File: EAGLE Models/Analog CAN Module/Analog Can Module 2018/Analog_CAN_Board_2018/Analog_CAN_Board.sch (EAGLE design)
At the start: 121 parts, among them IC1 AT90CAN128, IC10 OPA725DBV, IC11 OPA725DBV, IC12 OPA725DBV, IC13 OPA725DBV, IC2 MCP2551SO8, IC3 NUP2105L, IC4 OPA725DBV, IC5 FT232RL, IC6 MAX680CSA, IC7 OPA725DBV, IC8 OPA725DBV, IC9 OPA725DBV, Q1 56P2859, U11 LTC2053

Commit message: CAN Boards Finished
Passes DFM!
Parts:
- removed D1: 1N5819, diode:1N5819-B
- added U$4: 1N5819, diode:1N5819
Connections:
- net 12V: now also U$4.A; no longer D1.A
- net 5V_REG_IN: now also U$4.C; no longer D1.C
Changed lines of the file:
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@@
 <?xml version="1.0" encoding="utf-8"?>
 <!DOCTYPE eagle SYSTEM "eagle.dtd">
-<eagle version="8.4.2">
+<eagle version="8.3.2">
 <drawing>
 <settings>
@@
 <part name="D3" library="adafruit" deviceset="DIODE" device="SOD-123" value="1N4148"/>
 <part name="SJ2" library="SparkFun-Passives" deviceset="SOLDERJUMPER" device="NO"/>
-<part name="D1" library="diode" deviceset="1N581*" device="" technology="9-B" value="1N5819"/>
 <part name="U$26" library="on-semiconductor" deviceset="NCP1117" device=""/>
 <part name="C23" library="rcl" deviceset="C-US" device="C0603" value="10uF"/>
@@
 <part name="R37" library="SparkFun-Resistors" deviceset="RESISTOR" device="0603" value="0"/>
 <part name="U$1" library="us-te-con" deviceset="1734753-1_MINIUSB_CON" device=""/>
+<part name="U$4" library="diode" deviceset="1N5819" device=""/>
 </parts>
 <sheets>
@@
 <instance part="D3" gate="G$1" x="480.06" y="-106.68" rot="R90"/>
 <instance part="SJ2" gate="1" x="454.66" y="-114.3"/>
-<instance part="D1" gate="G$1" x="40.64" y="-30.48"/>
 <instance part="U$26" gate="G$1" x="78.74" y="-30.48"/>
 <instance part="C23" gate="G$1" x="50.8" y="-38.1"/>
@@
 <instance part="R37" gate="G$1" x="525.78" y="-40.64" rot="R270"/>
 <instance part="U$1" gate="G$1" x="378.46" y="-185.42"/>
+<instance part="U$4" gate="G$1" x="40.64" y="-30.48"/>
 </instances>
 <busses>
@@
 </segment>
 <segment>
-<pinref part="D1" gate="G$1" pin="A"/>
 <wire x1="38.1" y1="-30.48" x2="30.48" y2="-30.48" width="0.1524" layer="91"/>
 <label x="30.48" y="-30.48" size="1.778" layer="95" rot="R180" xref="yes"/>
+<pinref part="U$4" gate="G$1" pin="A"/>
 </segment>
 <segment>
@@
 <pinref part="U$26" gate="G$1" pin="INPUT"/>
 <wire x1="50.8" y1="-30.48" x2="63.5" y2="-30.48" width="0.1524" layer="91"/>
-<pinref part="D1" gate="G$1" pin="C"/>
 <wire x1="43.18" y1="-30.48" x2="50.8" y2="-30.48" width="0.1524" layer="91"/>
 <junction x="50.8" y="-30.48"/>
-</segment>
-</net>
+<pinref part="U$4" gate="G$1" pin="C"/>
+</segment>
+</net>

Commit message: Last minute CAN Board revision
- added 0 ohm resistors for filters and adjusted q to 2
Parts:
- added R36, R38, R39, R40, R41, R42, R43, R44: 0, SparkFun-Resistors:RESISTOR0603
- C14, C21, C27, C3, C35, C41, C45: value .1uF -> .0047uF
- C17, C26, C30, C44, C48, C6: value .33uF -> .1uF
- R1, R14, R17, R20, R26, R30, R33: value 3.9k -> 22k
- R16, R19, R22, R28, R29, R32, R35: value 5.1k -> 62k
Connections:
- net AGND: now also R36.2, R38.2, R39.2, R40.2, R41.2, R42.2, R43.2, R44.2
- net N$19: now also R36.1
- net N$26: now also R38.1
- net N$31: now also R39.1
- net N$38: now also R40.1
- net N$41: now also R44.1
- net N$44: now also R43.1
- net N$47: now also R42.1
- net N$50: now also R41.1
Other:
- moved on the sheet: C14, C15, C16, C17, C21, C22, C25, C26, C27, C28, C29, C3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

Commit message: Analog CAN Board Update
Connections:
- net AGND: now also U$3.B22, U$3.B23, U$3.B24; no longer U$3.B14, U$3.B15
- net DGND: now also U$3.B14, U$3.B15; no longer U$3.B22, U$3.B23, U$3.B24
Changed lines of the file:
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@@
-</segment>
-<segment>
-<pinref part="U$3" gate="G$1" pin="B14"/>
-<wire x1="495.3" y1="-15.24" x2="497.84" y2="-15.24" width="0.1524" layer="91"/>
-<label x="497.84" y="-15.24" size="1.778" layer="95"/>
-</segment>
-<segment>
-<pinref part="U$3" gate="G$1" pin="B15"/>
-<wire x1="495.3" y1="-20.32" x2="497.84" y2="-20.32" width="0.1524" layer="91"/>
-<label x="497.84" y="-20.32" size="1.778" layer="95"/>
 </segment>
 <segment>
@@
 <wire x1="347.98" y1="12.7" x2="342.9" y2="12.7" width="0.1524" layer="91"/>
 <label x="342.9" y="12.7" size="1.4224" layer="95" rot="R180" xref="yes"/>
+</segment>
+<segment>
+<pinref part="U$3" gate="G$1" pin="B24"/>
+<wire x1="495.3" y1="-66.04" x2="497.84" y2="-66.04" width="0.1524" layer="91"/>
+<label x="497.84" y="-66.04" size="1.778" layer="95"/>
+</segment>
+<segment>
+<pinref part="U$3" gate="G$1" pin="B23"/>
+<wire x1="495.3" y1="-60.96" x2="497.84" y2="-60.96" width="0.1524" layer="91"/>
+<label x="497.84" y="-60.96" size="1.778" layer="95"/>
+</segment>
+<segment>
+<pinref part="U$3" gate="G$1" pin="B22"/>
+<wire x1="495.3" y1="-55.88" x2="497.84" y2="-55.88" width="0.1524" layer="91"/>
+<label x="497.84" y="-55.88" size="1.778" layer="95"/>
 </segment>
 </net>
@@
 </segment>
 <segment>
-<pinref part="U$3" gate="G$1" pin="B22"/>
-<wire x1="495.3" y1="-55.88" x2="497.84" y2="-55.88" width="0.1524" layer="91"/>
-<label x="497.84" y="-55.88" size="1.778" layer="95"/>
-</segment>
-<segment>
-<pinref part="U$3" gate="G$1" pin="B23"/>
-<wire x1="495.3" y1="-60.96" x2="497.84" y2="-60.96" width="0.1524" layer="91"/>
-<label x="497.84" y="-60.96" size="1.778" layer="95"/>
-</segment>
-<segment>
-<pinref part="U$3" gate="G$1" pin="B24"/>
-<wire x1="495.3" y1="-66.04" x2="497.84" y2="-66.04" width="0.1524" layer="91"/>
-<label x="497.84" y="-66.04" size="1.778" layer="95"/>
-</segment>
-<segment>
 <pinref part="U$2" gate="G$1" pin="A"/>
 <wire x1="452.12" y1="-20.32" x2="444.5" y2="-20.32" width="0.1524" layer="91"/>
@@
 <label x="525.78" y="-58.42" size="1.27" layer="95" rot="R270" xref="yes"/>
 </segment>
+<segment>
+<pinref part="U$3" gate="G$1" pin="B14"/>
+<wire x1="495.3" y1="-15.24" x2="497.84" y2="-15.24" width="0.1524" layer="91"/>
+<label x="497.84" y="-15.24" size="1.778" layer="95"/>
+</segment>
+<segment>
+<pinref part="U$3" gate="G$1" pin="B15"/>
+<wire x1="495.3" y1="-20.32" x2="497.84" y2="-20.32" width="0.1524" layer="91"/>
+<label x="497.84" y="-20.32" size="1.778" layer="95"/>
+</segment>
 </net>

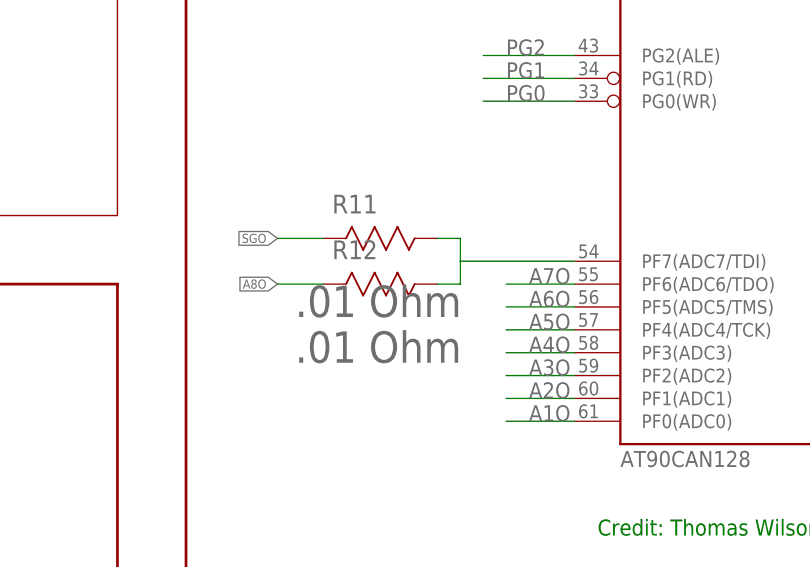
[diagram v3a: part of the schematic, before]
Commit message: Analog CAN Update
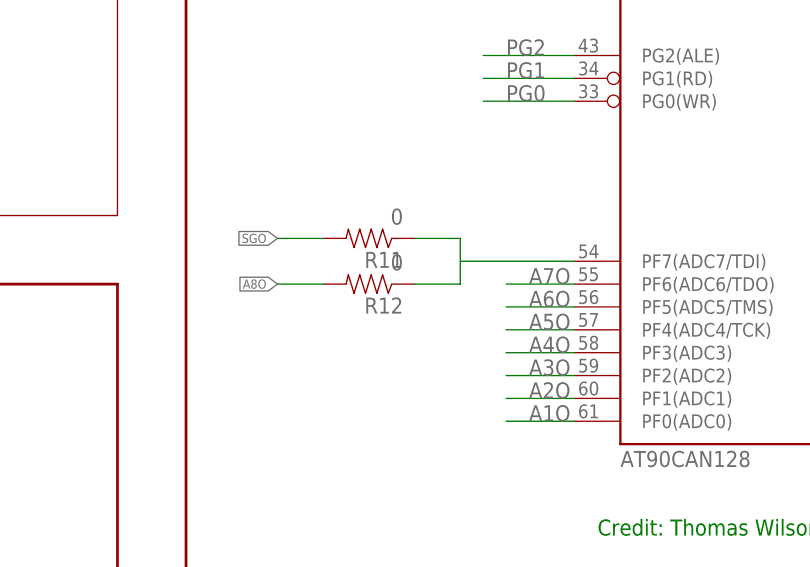
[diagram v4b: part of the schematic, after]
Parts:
- R11, R12: value .01 Ohm -> 0; device Vishay_By_element14_Batch_1:WSLP0603R0100FEA -> SparkFun-Resistors:RESISTOR0603
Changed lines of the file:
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@@
 <part name="R1" library="SparkFun-Resistors" deviceset="RESISTOR" device="0603" value="22k"/>
 <part name="C3" library="SparkFun-Passives" deviceset="CAP" device="0603-CAP" value=".0047uF"/>
-<part name="R11" library="Vishay_By_element14_Batch_1" deviceset="WSLP0603R0100FEA" device="" value=".01 Ohm"/>
-<part name="R12" library="Vishay_By_element14_Batch_1" deviceset="WSLP0603R0100FEA" device="" value=".01 Ohm"/>
 <part name="IC4" library="linear" deviceset="OPA725" device="DBV"/>
 <part name="R13" library="SparkFun-Resistors" deviceset="RESISTOR" device="0603" value="0"/>
@@
 <part name="R43" library="SparkFun-Resistors" deviceset="RESISTOR" device="0603" value="0"/>
 <part name="R44" library="SparkFun-Resistors" deviceset="RESISTOR" device="0603" value="0"/>
+<part name="R11" library="SparkFun-Resistors" deviceset="RESISTOR" device="0603" value="0"/>
+<part name="R12" library="SparkFun-Resistors" deviceset="RESISTOR" device="0603" value="0"/>
 </parts>
 <sheets>
@@
 <instance part="R1" gate="G$1" x="40.64" y="101.6" rot="R180"/>
 <instance part="C3" gate="G$1" x="50.8" y="93.98"/>
-<instance part="R11" gate="A" x="284.48" y="-119.38"/>
-<instance part="R12" gate="A" x="284.48" y="-124.46"/>
 <instance part="IC4" gate="G$1" x="66.04" y="99.06"/>
 <instance part="R13" gate="G$1" x="68.58" y="86.36" rot="R180"/>
@@
 <instance part="R43" gate="G$1" x="154.94" y="15.24" rot="R270"/>
 <instance part="R44" gate="G$1" x="58.42" y="15.24" rot="R270"/>
+<instance part="R11" gate="G$1" x="289.56" y="-119.38" rot="R180"/>
+<instance part="R12" gate="G$1" x="289.56" y="-124.46" rot="R180"/>
 </instances>
 <busses>
@@
 </segment>
 <segment>
-<pinref part="R11" gate="A" pin="2"/>
 <wire x1="284.48" y1="-119.38" x2="279.4" y2="-119.38" width="0.1524" layer="91"/>
 <label x="279.4" y="-119.38" size="1.016" layer="95" rot="R180" xref="yes"/>
+<pinref part="R11" gate="G$1" pin="2"/>
 </segment>
 </net>
@@
 <net name="N$18" class="0">
 <segment>
-<pinref part="R11" gate="A" pin="1"/>
-<wire x1="297.18" y1="-119.38" x2="299.72" y2="-119.38" width="0.1524" layer="91"/>
 <wire x1="299.72" y1="-119.38" x2="299.72" y2="-121.92" width="0.1524" layer="91"/>
-<pinref part="R12" gate="A" pin="1"/>
 <wire x1="299.72" y1="-121.92" x2="299.72" y2="-124.46" width="0.1524" layer="91"/>
-<wire x1="299.72" y1="-124.46" x2="297.18" y2="-124.46" width="0.1524" layer="91"/>
 <pinref part="IC1" gate="G$1" pin="PF7(ADC7/TDI)"/>
 <wire x1="299.72" y1="-121.92" x2="312.42" y2="-121.92" width="0.1524" layer="91"/>
+<pinref part="R11" gate="G$1" pin="1"/>
+<wire x1="294.64" y1="-119.38" x2="299.72" y2="-119.38" width="0.1524" layer="91"/>
+<pinref part="R12" gate="G$1" pin="1"/>
+<wire x1="294.64" y1="-124.46" x2="299.72" y2="-124.46" width="0.1524" layer="91"/>
 </segment>
 </net>
 <net name="A8O" class="0">
 <segment>
-<pinref part="R12" gate="A" pin="2"/>
 <wire x1="284.48" y1="-124.46" x2="279.4" y2="-124.46" width="0.1524" layer="91"/>
 <label x="279.4" y="-124.46" size="1.016" layer="95" rot="R180" xref="yes"/>
-</segment>
-<segment>
+<pinref part="R12" gate="G$1" pin="2"/>
+</segment>
+<segment>

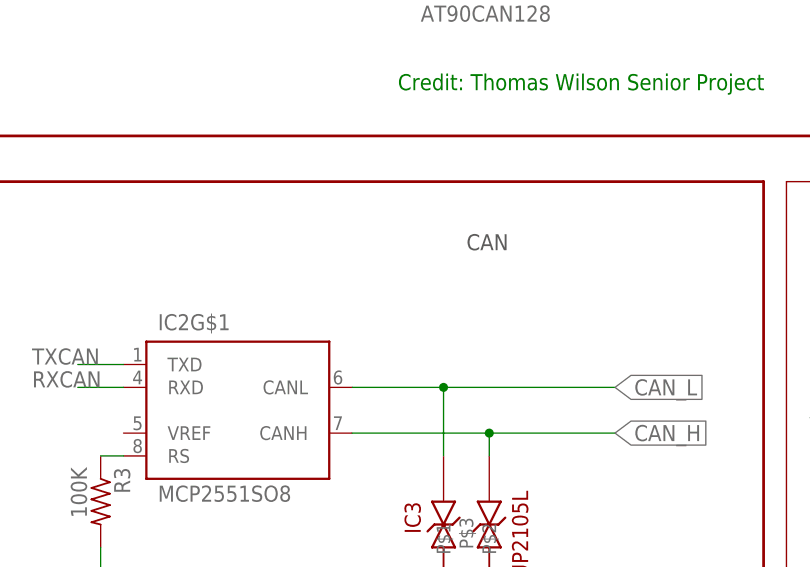
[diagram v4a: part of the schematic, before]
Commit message: Fixed ground issue on the can transceiver
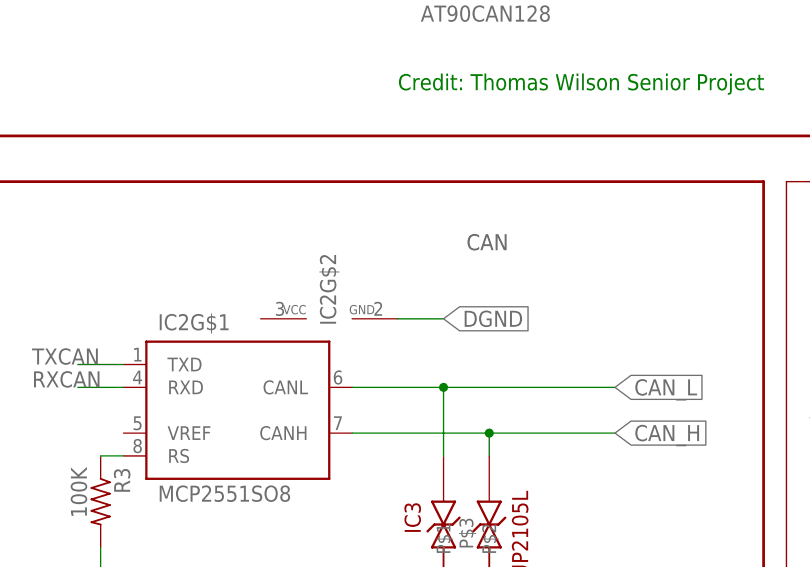
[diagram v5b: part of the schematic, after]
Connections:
- net DGND: now also IC2G$2.GND
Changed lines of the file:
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@@
 <?xml version="1.0" encoding="utf-8"?>
 <!DOCTYPE eagle SYSTEM "eagle.dtd">
-<eagle version="8.3.2">
+<eagle version="8.4.3">
 <drawing>
 <settings>
@@
 <grid distance="0.1" unitdist="inch" unit="inch" style="lines" multiple="1" display="no" altdistance="0.01" altunitdist="inch" altunit="inch"/>
 <layers>
-<layer number="1" name="Top" color="4" fill="1" visible="no" active="no"/>
-<layer number="2" name="Route2" color="1" fill="3" visible="no" active="no"/>
-<layer number="3" name="Route3" color="4" fill="3" visible="no" active="no"/>
-<layer number="4" name="Route4" color="1" fill="4" visible="no" active="no"/>
-<layer number="5" name="Route5" color="4" fill="4" visible="no" active="no"/>
-<layer number="6" name="Route6" color="10" fill="1" visible="no" active="no"/>
-<layer number="7" name="Route7" color="4" fill="8" visible="no" active="no"/>
-<layer number="8" name="Route8" color="1" fill="2" visible="no" active="no"/>
-<layer number="9" name="Route9" color="4" fill="2" visible="no" active="no"/>
-<layer number="10" name="Route10" color="1" fill="7" visible="no" active="no"/>
-<layer number="11" name="Route11" color="11" fill="1" visible="no" active="no"/>
-<layer number="12" name="Route12" color="1" fill="5" visible="no" active="no"/>
-<layer number="13" name="Route13" color="4" fill="5" visible="no" active="no"/>
-<layer number="14" name="Route14" color="1" fill="6" visible="no" active="no"/>
-<layer number="15" name="Route15" color="4" fill="6" visible="no" active="no"/>
-<layer number="16" name="Bottom" color="1" fill="1" visible="no" active="no"/>
-<layer number="17" name="Pads" color="2" fill="1" visible="no" active="no"/>
-<layer number="18" name="Vias" color="2" fill="1" visible="no" active="no"/>
-<layer number="19" name="Unrouted" color="6" fill="1" visible="no" active="no"/>
-<layer number="20" name="Dimension" color="24" fill="1" visible="no" active="no"/>
-<layer number="21" name="tPlace" color="7" fill="1" visible="no" active="no"/>
-<layer number="22" name="bPlace" color="7" fill="1" visible="no" active="no"/>
-<layer number="23" name="tOrigins" color="15" fill="1" visible="no" active="no"/>
-<layer number="24" name="bOrigins" color="15" fill="1" visible="no" active="no"/>
-<layer number="25" name="tNames" color="7" fill="1" visible="no" active="no"/>
-<layer number="26" name="bNames" color="7" fill="1" visible="no" active="no"/>
-<layer number="27" name="tValues" color="7" fill="1" visible="no" active="no"/>
-<layer number="28" name="bValues" color="7" fill="1" visible="no" active="no"/>
+<layer number="1" name="Top" color="4" fill="1" visible="yes" active="no"/>
+<layer number="2" name="Route2" color="1" fill="3" visible="yes" active="no"/>
+<layer number="3" name="Route3" color="4" fill="3" visible="yes" active="no"/>
+<layer number="4" name="Route4" color="1" fill="4" visible="yes" active="no"/>
+<layer number="5" name="Route5" color="4" fill="4" visible="yes" active="no"/>
+<layer number="6" name="Route6" color="10" fill="1" visible="yes" active="no"/>
+<layer number="7" name="Route7" color="4" fill="8" visible="yes" active="no"/>
+<layer number="8" name="Route8" color="1" fill="2" visible="yes" active="no"/>
+<layer number="9" name="Route9" color="4" fill="2" visible="yes" active="no"/>
+<layer number="10" name="Route10" color="1" fill="7" visible="yes" active="no"/>
+<layer number="11" name="Route11" color="11" fill="1" visible="yes" active="no"/>
+<layer number="12" name="Route12" color="1" fill="5" visible="yes" active="no"/>
+<layer number="13" name="Route13" color="4" fill="5" visible="yes" active="no"/>
+<layer number="14" name="Route14" color="1" fill="6" visible="yes" active="no"/>
+<layer number="15" name="Route15" color="4" fill="6" visible="yes" active="no"/>
+<layer number="16" name="Bottom" color="1" fill="1" visible="yes" active="no"/>
+<layer number="17" name="Pads" color="2" fill="1" visible="yes" active="no"/>
+<layer number="18" name="Vias" color="2" fill="1" visible="yes" active="no"/>
+<layer number="19" name="Unrouted" color="6" fill="1" visible="yes" active="no"/>
+<layer number="20" name="Dimension" color="24" fill="1" visible="yes" active="no"/>
+<layer number="21" name="tPlace" color="7" fill="1" visible="yes" active="no"/>
+<layer number="22" name="bPlace" color="7" fill="1" visible="yes" active="no"/>
+<layer number="23" name="tOrigins" color="15" fill="1" visible="yes" active="no"/>
+<layer number="24" name="bOrigins" color="15" fill="1" visible="yes" active="no"/>
+<layer number="25" name="tNames" color="7" fill="1" visible="yes" active="no"/>
+<layer number="26" name="bNames" color="7" fill="1" visible="yes" active="no"/>
+<layer number="27" name="tValues" color="7" fill="1" visible="yes" active="no"/>
+<layer number="28" name="bValues" color="7" fill="1" visible="yes" active="no"/>
 <layer number="29" name="tStop" color="7" fill="3" visible="no" active="no"/>
 <layer number="30" name="bStop" color="7" fill="6" visible="no" active="no"/>
@@
 <layer number="35" name="tGlue" color="7" fill="4" visible="no" active="no"/>
 <layer number="36" name="bGlue" color="7" fill="5" visible="no" active="no"/>
-<layer number="37" name="tTest" color="7" fill="1" visible="no" active="no"/>
-<layer number="38" name="bTest" color="7" fill="1" visible="no" active="no"/>
+<layer number="37" name="tTest" color="7" fill="1" visible="yes" active="no"/>
+<layer number="38" name="bTest" color="7" fill="1" visible="yes" active="no"/>
 <layer number="39" name="tKeepout" color="4" fill="11" visible="no" active="no"/>
 <layer number="40" name="bKeepout" color="1" fill="11" visible="no" active="no"/>
@@
 <layer number="44" name="Drills" color="7" fill="1" visible="no" active="no"/>
 <layer number="45" name="Holes" color="7" fill="1" visible="no" active="no"/>
-<layer number="46" name="Milling" color="3" fill="1" visible="no" active="no"/>
-<layer number="47" name="Measures" color="7" fill="1" visible="no" active="no"/>
-<layer number="48" name="Document" color="7" fill="1" visible="no" active="no"/>
-<layer number="49" name="Reference" color="7" fill="1" visible="no" active="no"/>
-<layer number="50" name="dxf" color="7" fill="1" visible="no" active="no"/>
-<layer number="51" name="tDocu" color="7" fill="1" visible="no" active="no"/>
-<layer number="52" name="bDocu" color="7" fill="1" visible="no" active="no"/>
-<layer number="53" name="tGND_GNDA" color="7" fill="9" visible="no" active="no"/>
-<layer number="54" name="bGND_GNDA" color="1" fill="9" visible="no" active="no"/>
-<layer number="56" name="wert" color="7" fill="1" visible="no" active="no"/>
-<layer number="57" name="tCAD" color="7" fill="1" visible="no" active="no"/>
+<layer number="46" name="Milling" color="3" fill="1" visible="yes" active="no"/>
+<layer number="47" name="Measures" color="7" fill="1" visible="yes" active="no"/>
+<layer number="48" name="Document" color="7" fill="1" visible="yes" active="no"/>
+<layer number="49" name="Reference" color="7" fill="1" visible="yes" active="no"/>
+<layer number="50" name="dxf" color="7" fill="1" visible="yes" active="no"/>
+<layer number="51" name="tDocu" color="7" fill="1" visible="yes" active="no"/>
+<layer number="52" name="bDocu" color="7" fill="1" visible="yes" active="no"/>
+<layer number="53" name="tGND_GNDA" color="7" fill="9" visible="yes" active="no"/>
+<layer number="54" name="bGND_GNDA" color="1" fill="9" visible="yes" active="no"/>
+<layer number="56" name="wert" color="7" fill="1" visible="yes" active="no"/>
+<layer number="57" name="tCAD" color="7" fill="1" visible="yes" active="no"/>
 <layer number="90" name="Modules" color="5" fill="1" visible="yes" active="yes"/>
 <layer number="91" name="Nets" color="2" fill="1" visible="yes" active="yes"/>
@@
 <instance part="R11" gate="G$1" x="289.56" y="-119.38" rot="R180"/>
 <instance part="R12" gate="G$1" x="289.56" y="-124.46" rot="R180"/>
+<instance part="IC2" gate="G$2" x="307.34" y="-177.8" rot="R90"/>
 </instances>
 <busses>
@@
 <label x="497.84" y="-20.32" size="1.778" layer="95"/>
 </segment>
-</net>
+<segment>
+<pinref part="IC2" gate="G$2" pin="GND"/>
+<wire x1="314.96" y1="-177.8" x2="320.04" y2="-177.8" width="0.1524" layer="91"/>
+<label x="320.04" y="-177.8" size="1.778" layer="95" xref="yes"/>
+</segment>
+</net>

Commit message: Analog CAN Board Updates/Reference designators
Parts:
- IC15: value REG-104GA-5 -> IC15
- renumbered H7 to J3, U$1 to J1, U$10V2V5 to IC16, U$2 to D5, U$26 to IC14, U$3 to J2, U$4 to D6, U$5 to IC15, U11 to IC17, VCC! to LED4
